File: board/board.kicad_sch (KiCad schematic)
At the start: 144 parts, among them K1 KEYSW, K10 KEYSW, K11 KEYSW, K12 KEYSW, K13 KEYSW, K14 KEYSW, K15 KEYSW, K16 KEYSW, K17 KEYSW, K18 KEYSW, K19 KEYSW, K2 KEYSW, K20 KEYSW, K21 KEYSW, K22 KEYSW, K23 KEYSW, K24 KEYSW, K25 KEYSW, K26 KEYSW, K27 KEYSW, K28 KEYSW, K29 KEYSW, K3 KEYSW, K30 KEYSW, K31 KEYSW, K32 KEYSW, K33 KEYSW, K34 KEYSW, K35 KEYSW, K36 KEYSW, K37 KEYSW, K38 KEYSW, K39 KEYSW, K4 KEYSW, K40 KEYSW, K41 KEYSW, K42 KEYSW, K43 KEYSW, K44 KEYSW, K45 KEYSW, K46 KEYSW, K47 KEYSW, K48 KEYSW, K49 KEYSW, K5 KEYSW, K50 KEYSW, K51 KEYSW, K52 KEYSW, K53 KEYSW, K54 KEYSW, K55 KEYSW, K56 KEYSW, K57 KEYSW, K58 KEYSW, K59 KEYSW, K6 KEYSW, K60 KEYSW, K61 KEYSW, K62 KEYSW, K63 KEYSW, K64 KEYSW, K65 KEYSW, K66 KEYSW, K67 KEYSW, K68 KEYSW, K69 KEYSW, K7 KEYSW, K70 KEYSW, K8 KEYSW, K9 KEYSW, U1 ATMEGA32U4, X1 XTAL_GND

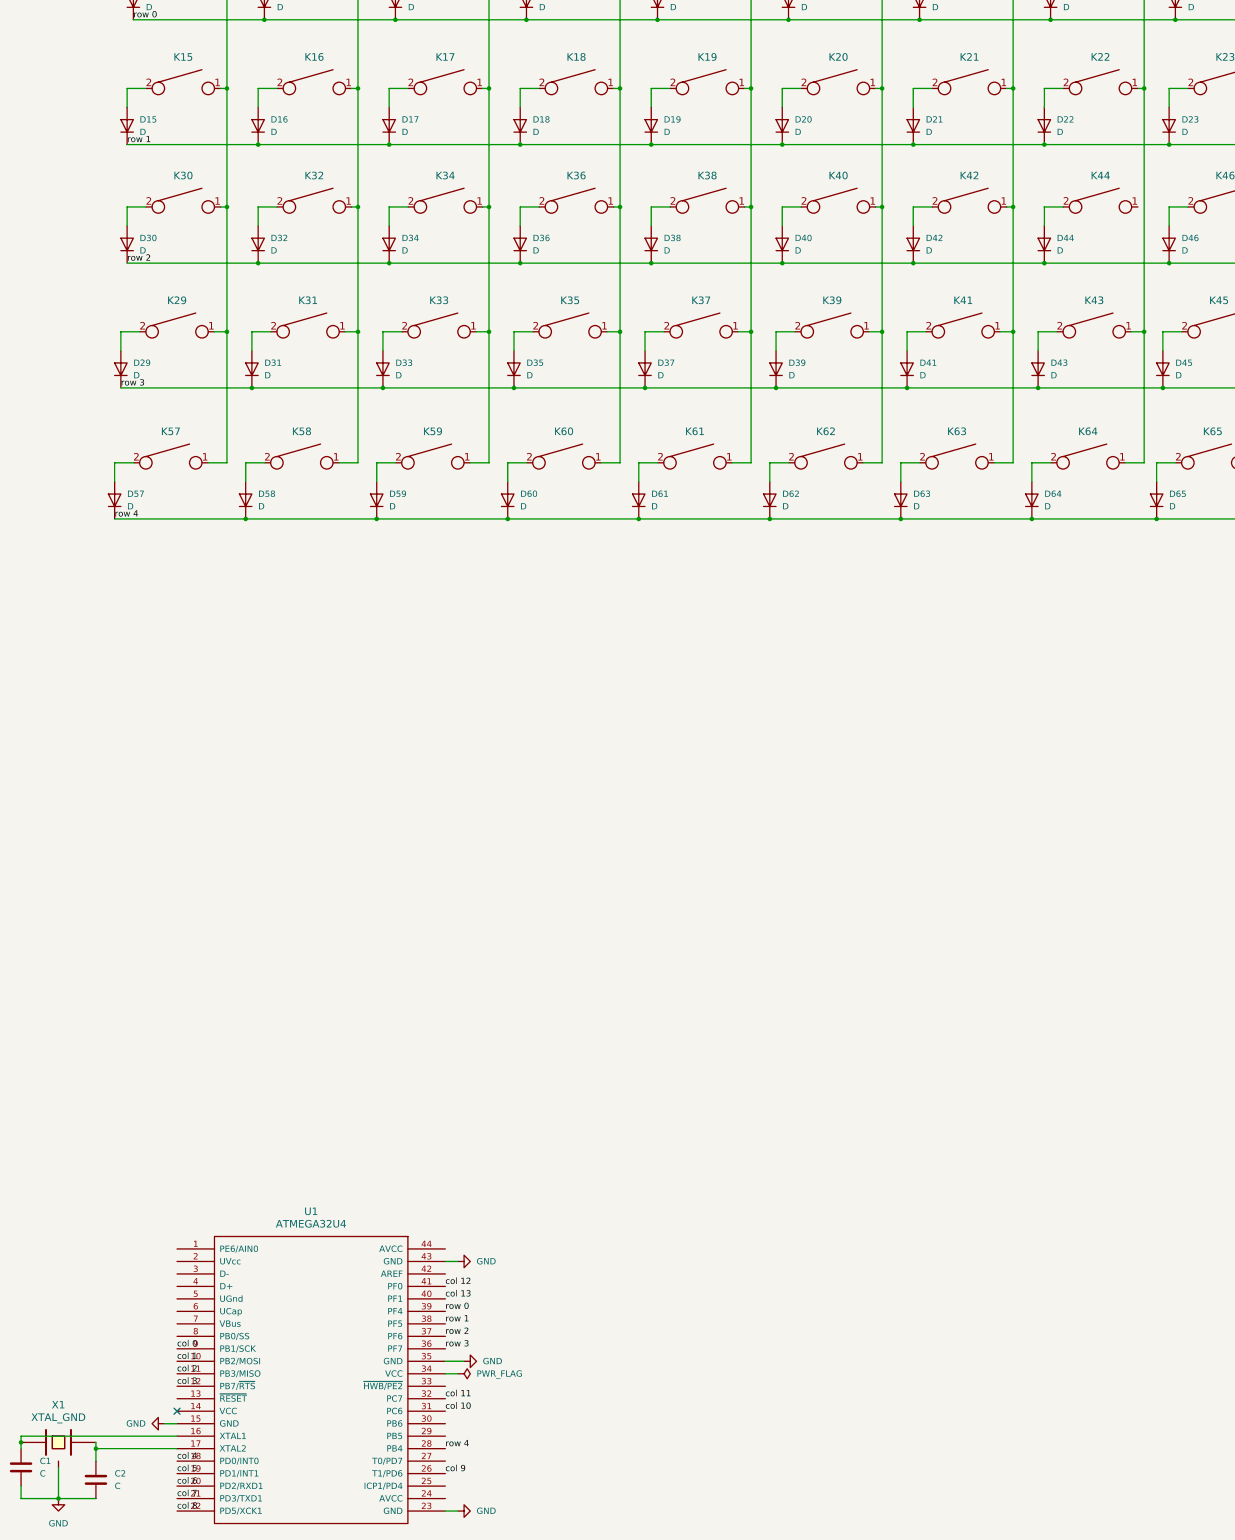
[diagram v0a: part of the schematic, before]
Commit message: microcontroller wiring, diode and switch footprints assigned, led on plug in
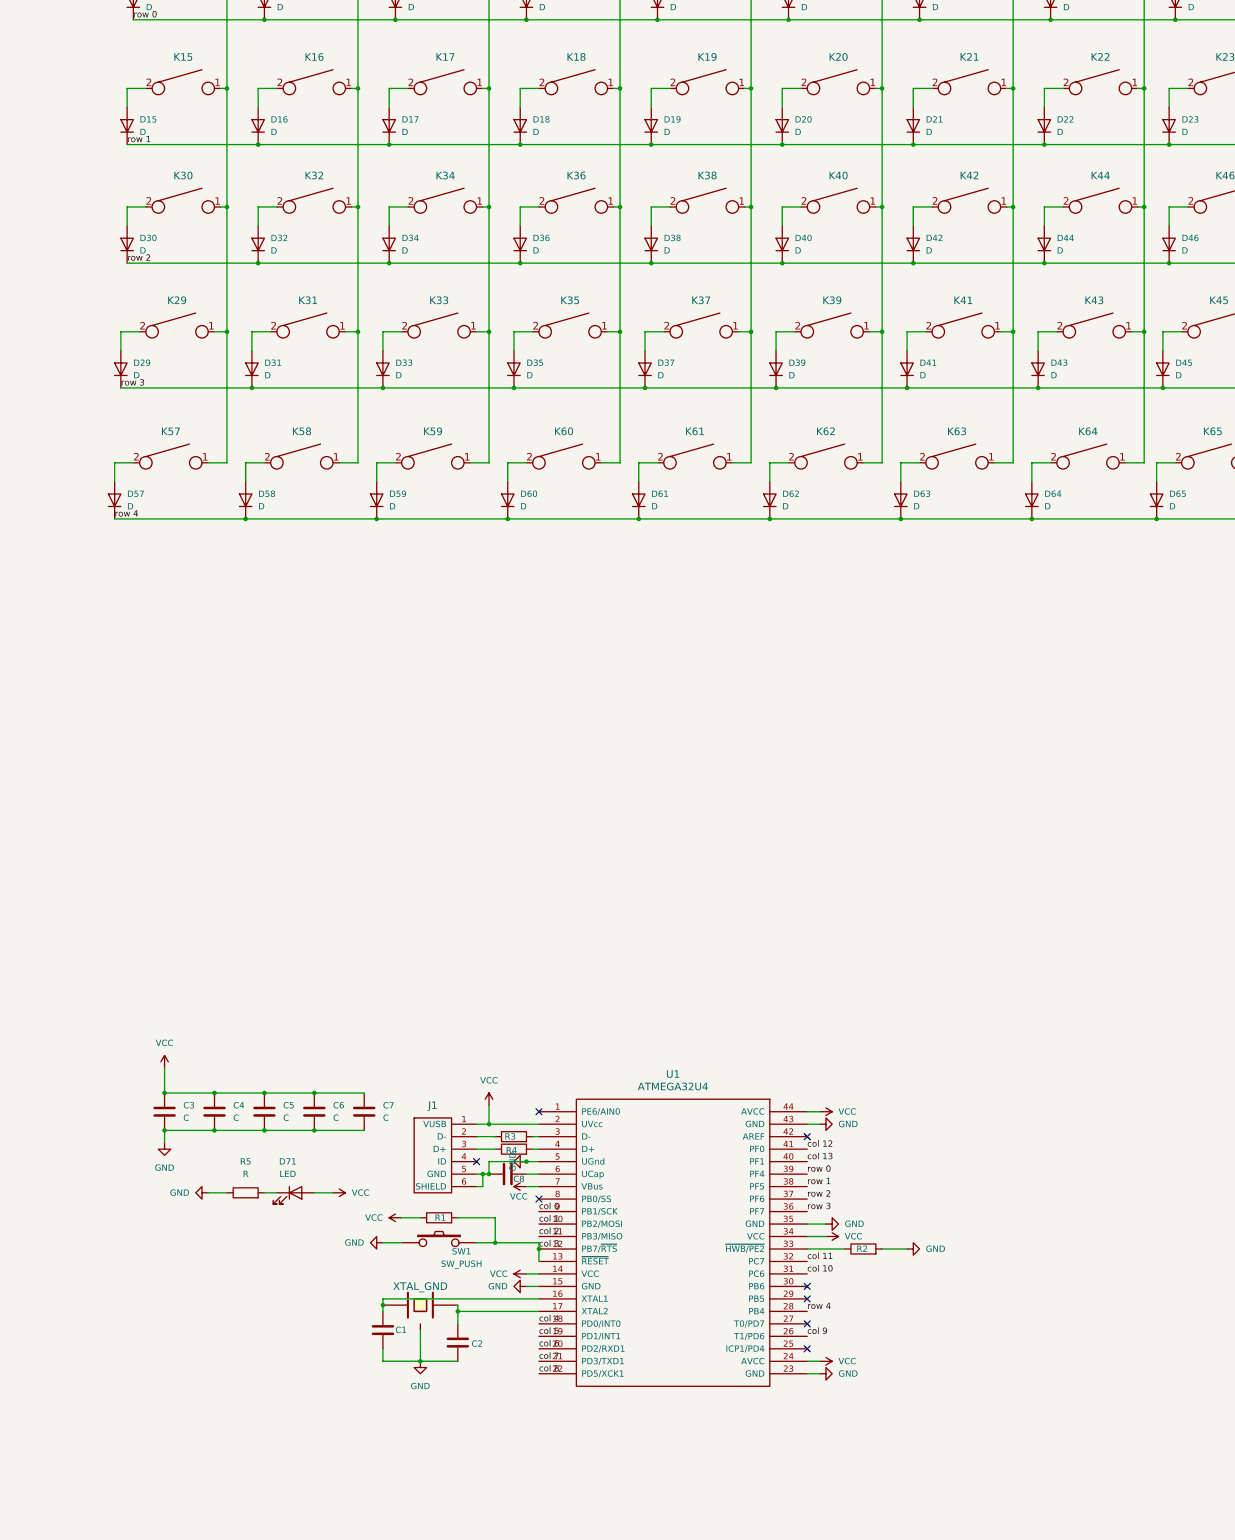
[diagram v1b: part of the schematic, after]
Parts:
- added C3, C4, C5, C6, C7, C8: C, symbol Device:C
- added D71: LED, symbol Device:LED
- added J1: USB_mini_micro_B, symbol keyboard_parts:USB_mini_micro_B
- added R1, R2, R3, R4, R5: R, symbol Device:R
- added SW1: SW_PUSH, symbol keyboard_parts:SW_PUSH
- D1, D10, D11, D12, D13, D14, D15, D16, D17, D18, D19, D2, D20, D21, D22, D23, D24, D25, D26, D27, D28, D29, D3, D30, D31, D32, D33, D34, D35, D36, D37, D38, D39, D4, D40, D41, D42, D43, D44, D45, D46, D47, D48, D49, D5, D50, D51, D52, D53, D54, D55, D56, D57, D58, D59, D6, D60, D61, D62, D63, D64, D65, D66, D67, D68, D69, D7, D70, D8, D9: footprint (none) -> Diode_SMD:D_SOD-123
- K1, K10, K11, K12, K13, K14, K15, K16, K17, K18, K19, K2, K20, K21, K22, K23, K24, K25, K26, K27, K28, K29, K3, K30, K31, K32, K33, K34, K35, K36, K37, K38, K39, K4, K40, K41, K42, K43, K44, K45, K46, K47, K48, K49, K5, K50, K51, K52, K53, K54, K55, K56, K57, K58, K59, K6, K60, K61, K62, K63, K64, K65, K66, K67, K68, K69, K7, K70, K8, K9: footprint (none) -> Button_Switch_Keyboard:SW_Cherry_MX_1.00u_PCB
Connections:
- net GND: now also U1.5 (UGnd), C3.2, C4.2, C5.2, C6.2, C7.2, C8.1, J1.5 (GND), J1.6 (SHIELD), R2.2, R5.1, SW1.1
- net col 3: now also U1.13 (~{RESET}), R1.2, SW1.2
- net col 7: now also K44.1
- net VCC: now reaches U1.14 (VCC)
- net VCC: now also U1.2 (UVcc), U1.24 (AVCC), U1.34 (VCC), U1.44 (AVCC), U1.7 (VBus), C3.1, C4.1, C5.1, C6.1, C7.1, D71.2 (A), J1.1 (VUSB), R1.1
- net at U1.3 (D-): now also R3.2
- net at U1.33 (~{HWB/PE2}): now also R2.1
- net at U1.4 (D+): now also R4.2
- net at U1.6 (UCap): now also C8.2
- new net: D71.1 (K), R5.2
- new net: J1.3 (D+), R4.1
- new net: J1.2 (D-), R3.1
- no-connect marks 1 -> 8
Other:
- moved on the sheet: C1, C2, U1
